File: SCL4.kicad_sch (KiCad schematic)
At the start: 38 parts, among them J1 spare1, J2 spare2, J3 Siemens_A1010-A263, J4 SP1, J5 SP2, J6 Conn_01x08, J7 5V out, U1 MC3487DX, U2 MC3487DX, U3 TRAM Size 2, U4 MC10H125 (20PLCC), U5 MC10H124 (20PLCC)

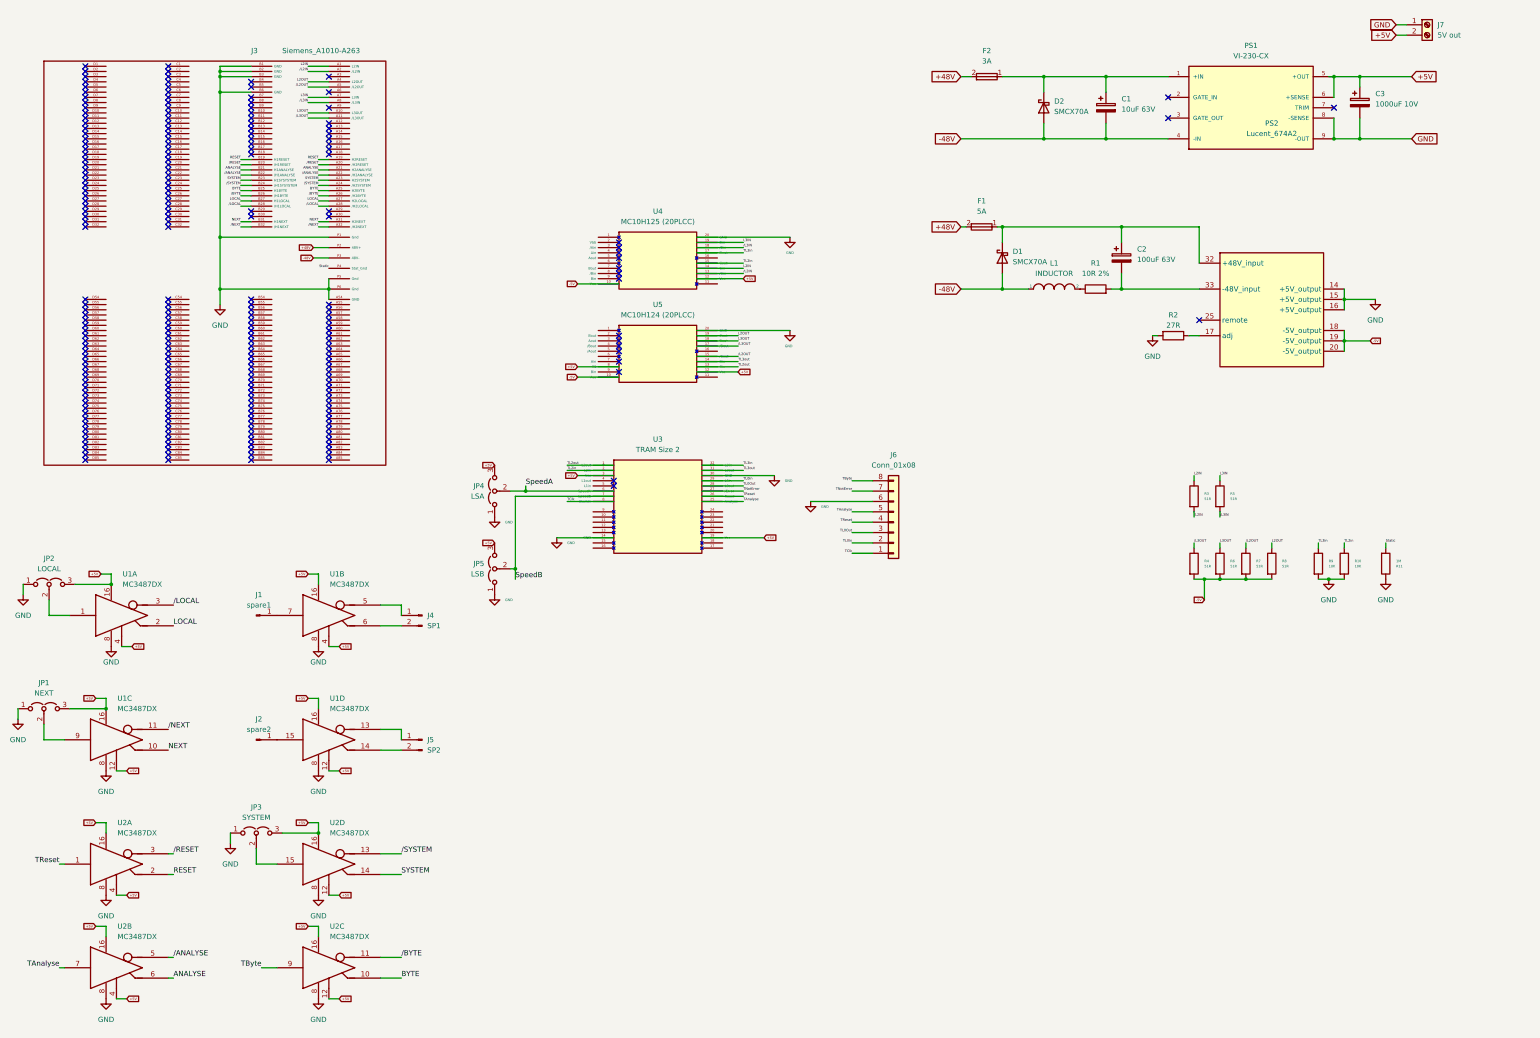
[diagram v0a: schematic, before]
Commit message: update 256pin connector
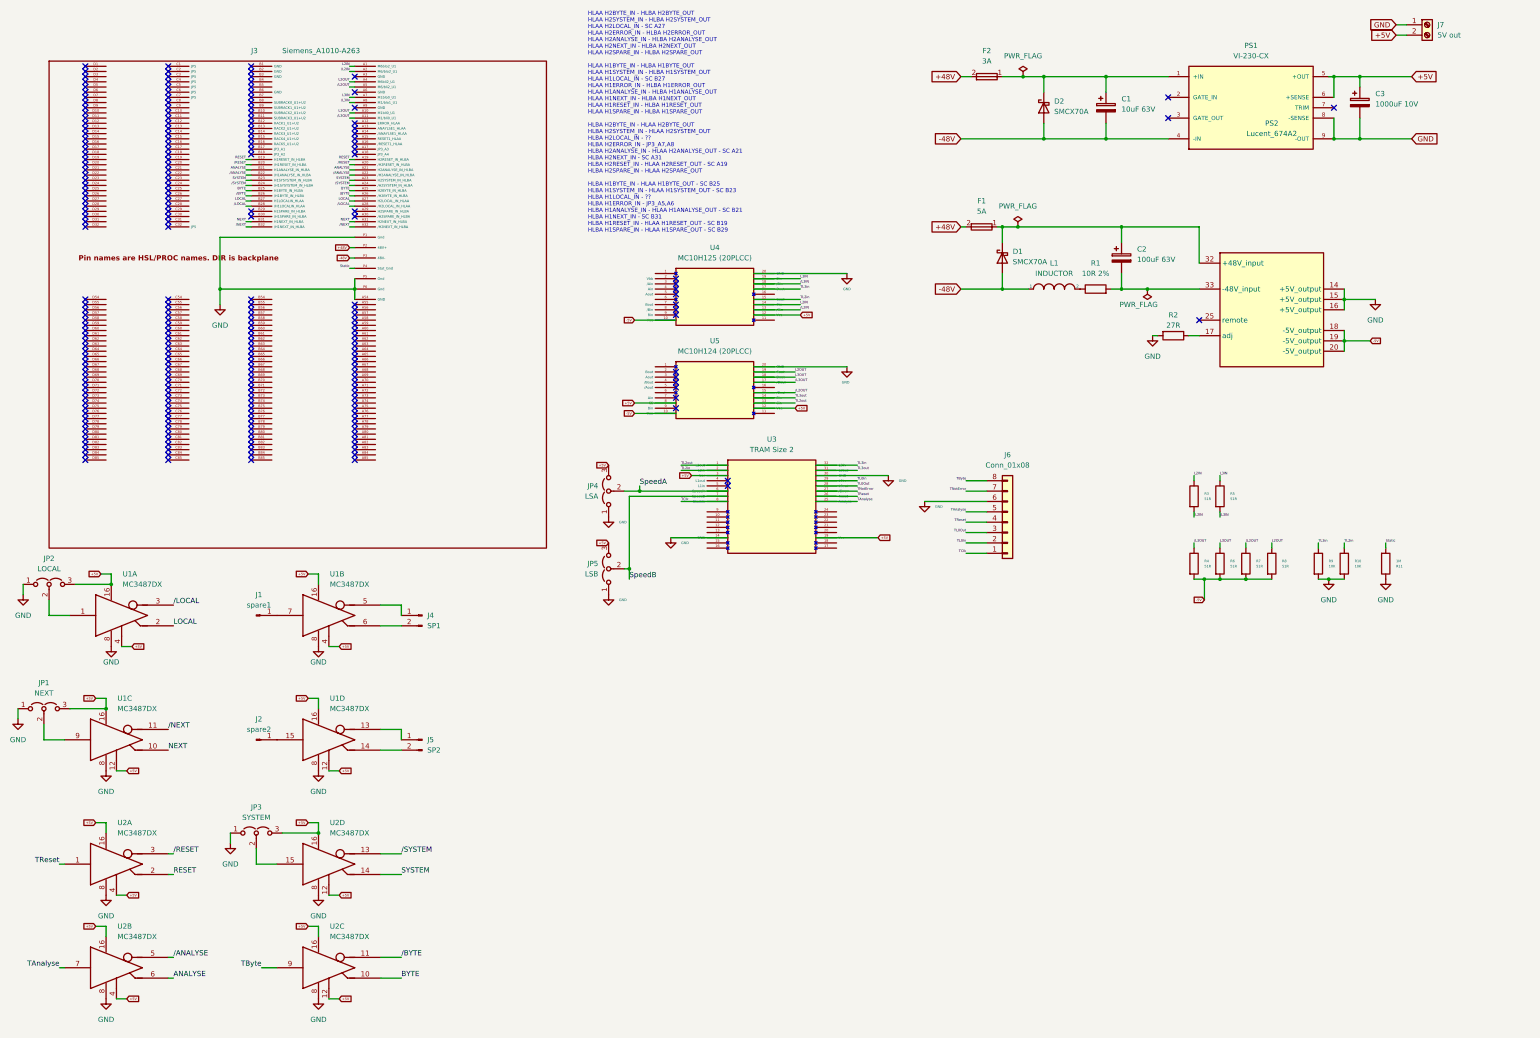
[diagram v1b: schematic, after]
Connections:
- net GND: no longer J3.B1 (GND), J3.B2 (GND), J3.B3 (GND), J3.B6 (GND)
- no-connect marks 238 -> 242
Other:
- note added: "HLAA H2BYTE_IN - HLBA H2BYTE_OUT HLAA H2SYSTEM_IN - HLBA H2SYSTEM_OUT HLAA H2LOCAL_IN - SC A27 HLAA H2ERROR_IN - HLBA H2ERROR_OUT HLAA H2ANALYSE_IN - HLBA H2ANALYSE_OUT HLAA H2NEXT_IN - HLBA H2NEXT_OUT HLAA H2SPARE_IN - HLBA H2SPARE_OUT HLAA H1BYTE_IN - HLBA H1BYTE_OUT HLAA H1SYSTEM_IN - HLBA H1SYSTEM_OUT HLAA H1LOCAL_IN - SC B27 HLAA H1ERROR_IN - HLBA H1ERROR_OUT HLAA H1ANALYSE_IN - HLBA H1ANALY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"
- moved on the sheet: J6, JP4, JP5, U3, U4, U5

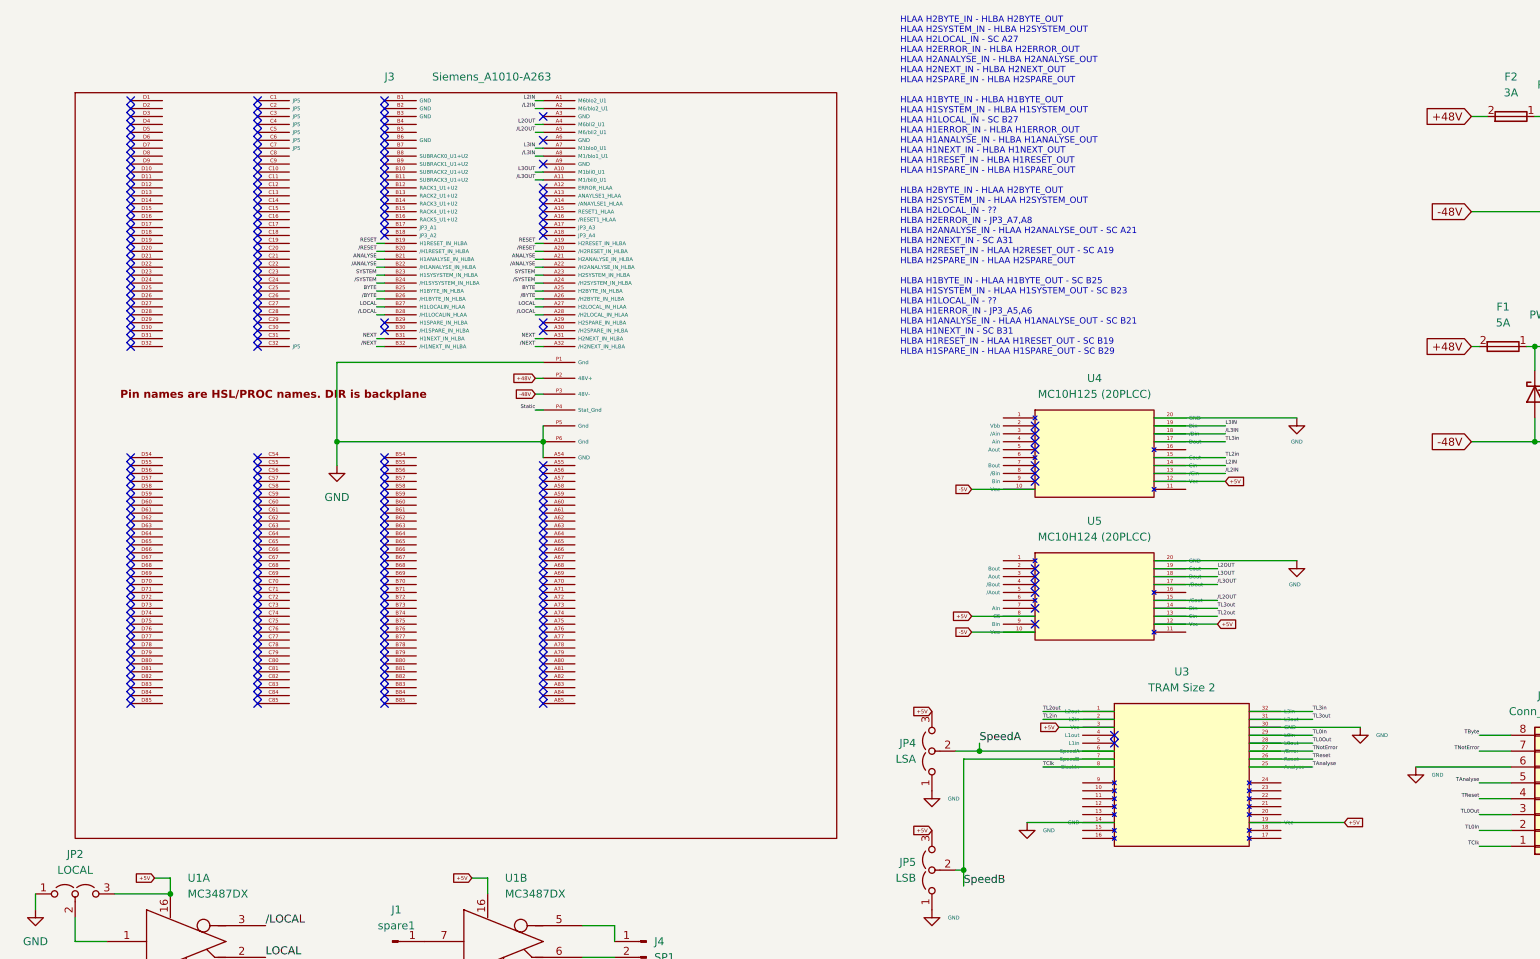
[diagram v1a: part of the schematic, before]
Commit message: more SCL pins named
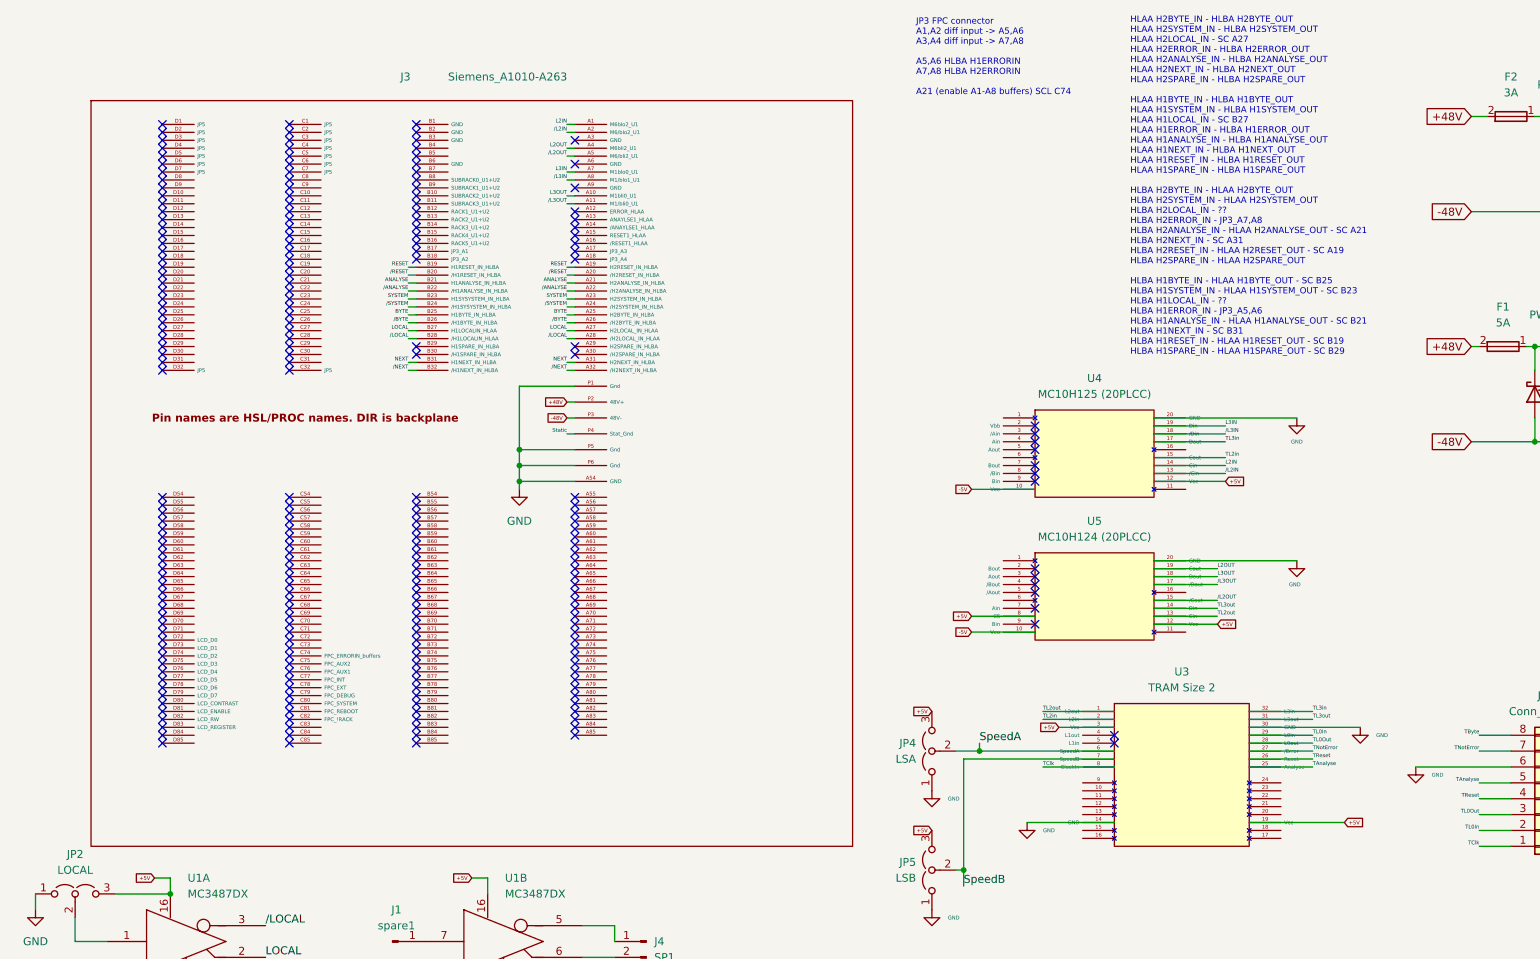
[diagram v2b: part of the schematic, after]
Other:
- note added: "JP3 FPC connector A1,A2 diff input -> A5,A6 A3,A4 diff input -> A7,A8 A5,A6 HLBA H1ERRORIN A7,A8 HLBA H2ERRORIN A21 (enable A1-A8 buffers) SCL C74"

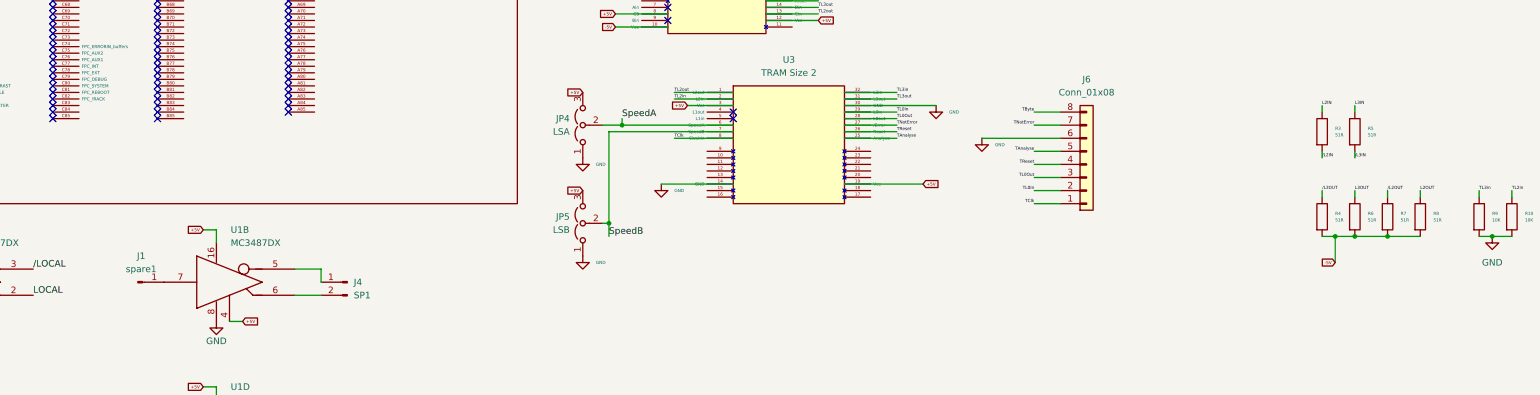
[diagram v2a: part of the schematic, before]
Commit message: Add HLAA enable jumper
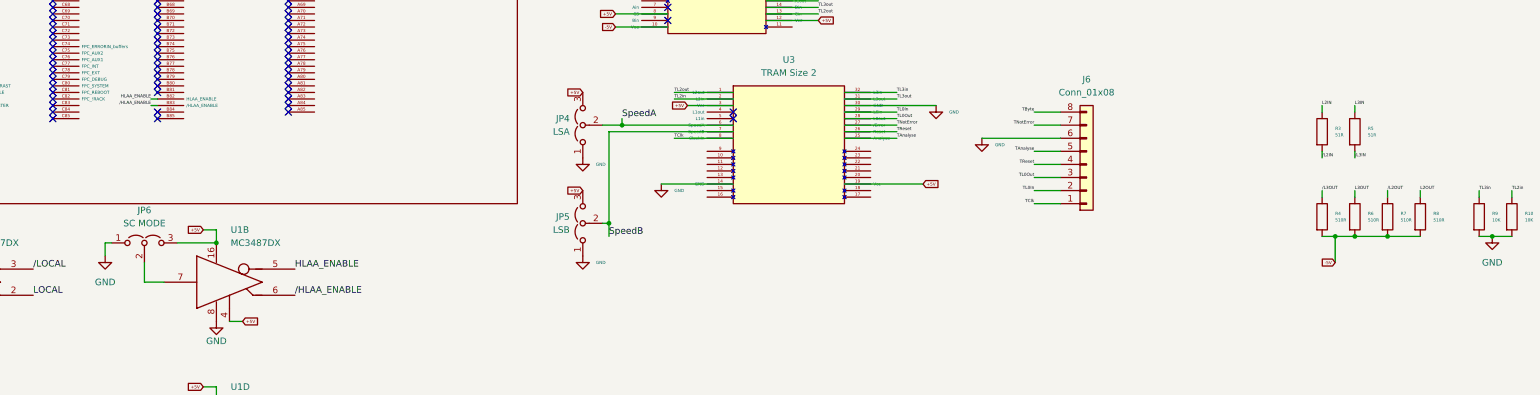
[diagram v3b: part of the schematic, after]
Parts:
- removed J1: spare1, Connector_PinHeader_2.54mm:PinHeader_1x01_P2.54mm_Vertical, symbol Connector:Conn_01x01_Male
- removed J4: SP1, Connector_PinHeader_2.54mm:PinHeader_1x02_P2.54mm_Vertical, symbol Connector:Conn_01x02_Male
- added JP6: SC MODE, Connector_PinHeader_2.54mm:PinHeader_1x03_P2.54mm_Vertical, symbol Jumper:Jumper_3_Open
- R4, R6, R7, R8: value 51R -> 510R
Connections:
- net +5V: now also JP6.3 (B)
- net GND: now also JP6.1 (A)
- net HLAA_ENABLE: now reaches J3.B82 (HLAA_ENABLE)
- net HLAA_ENABLE: now also U1.5 (OUT-)
- net /HLAA_ENABLE: now reaches J3.B83 (/HLAA_ENABLE)
- net /HLAA_ENABLE: now also U1.6 (OUT+)
- net at U1.7 (INPUT): now also JP6.2 (C)
- no-connect marks 242 -> 240
